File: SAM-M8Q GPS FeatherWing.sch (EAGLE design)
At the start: 24 parts, among them Q1 DMG3415U-7, Q2 2N2222, SW1 KMR2, U1 SAM-M8Q

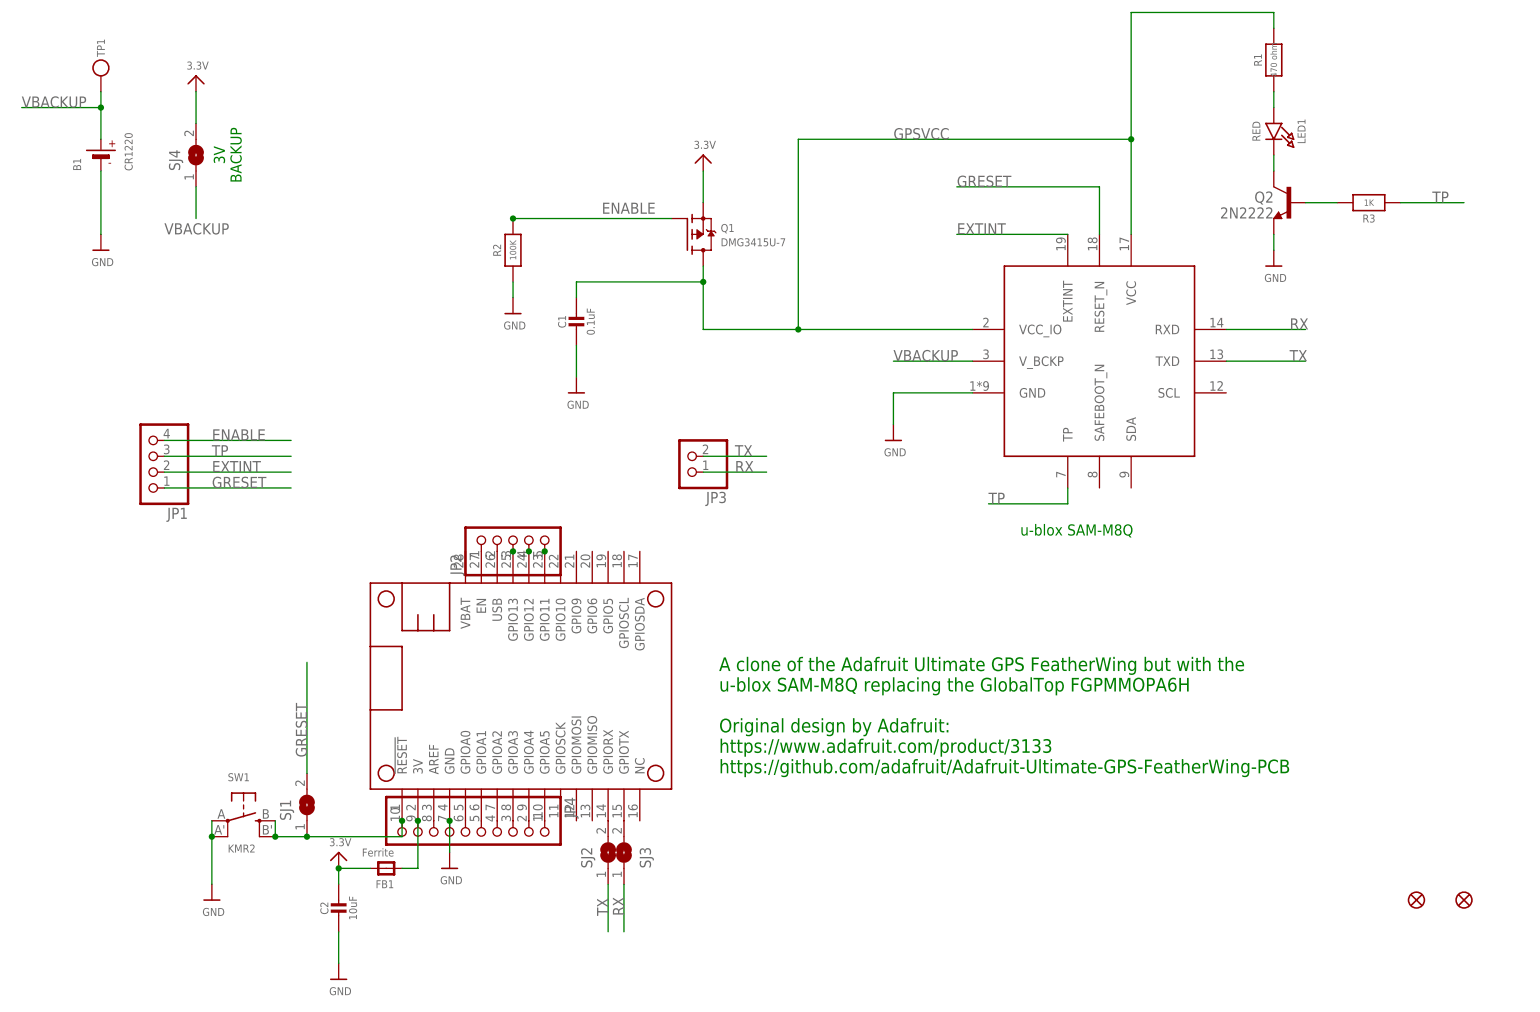
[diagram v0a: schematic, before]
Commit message: Minor tweaks. Included BOM.
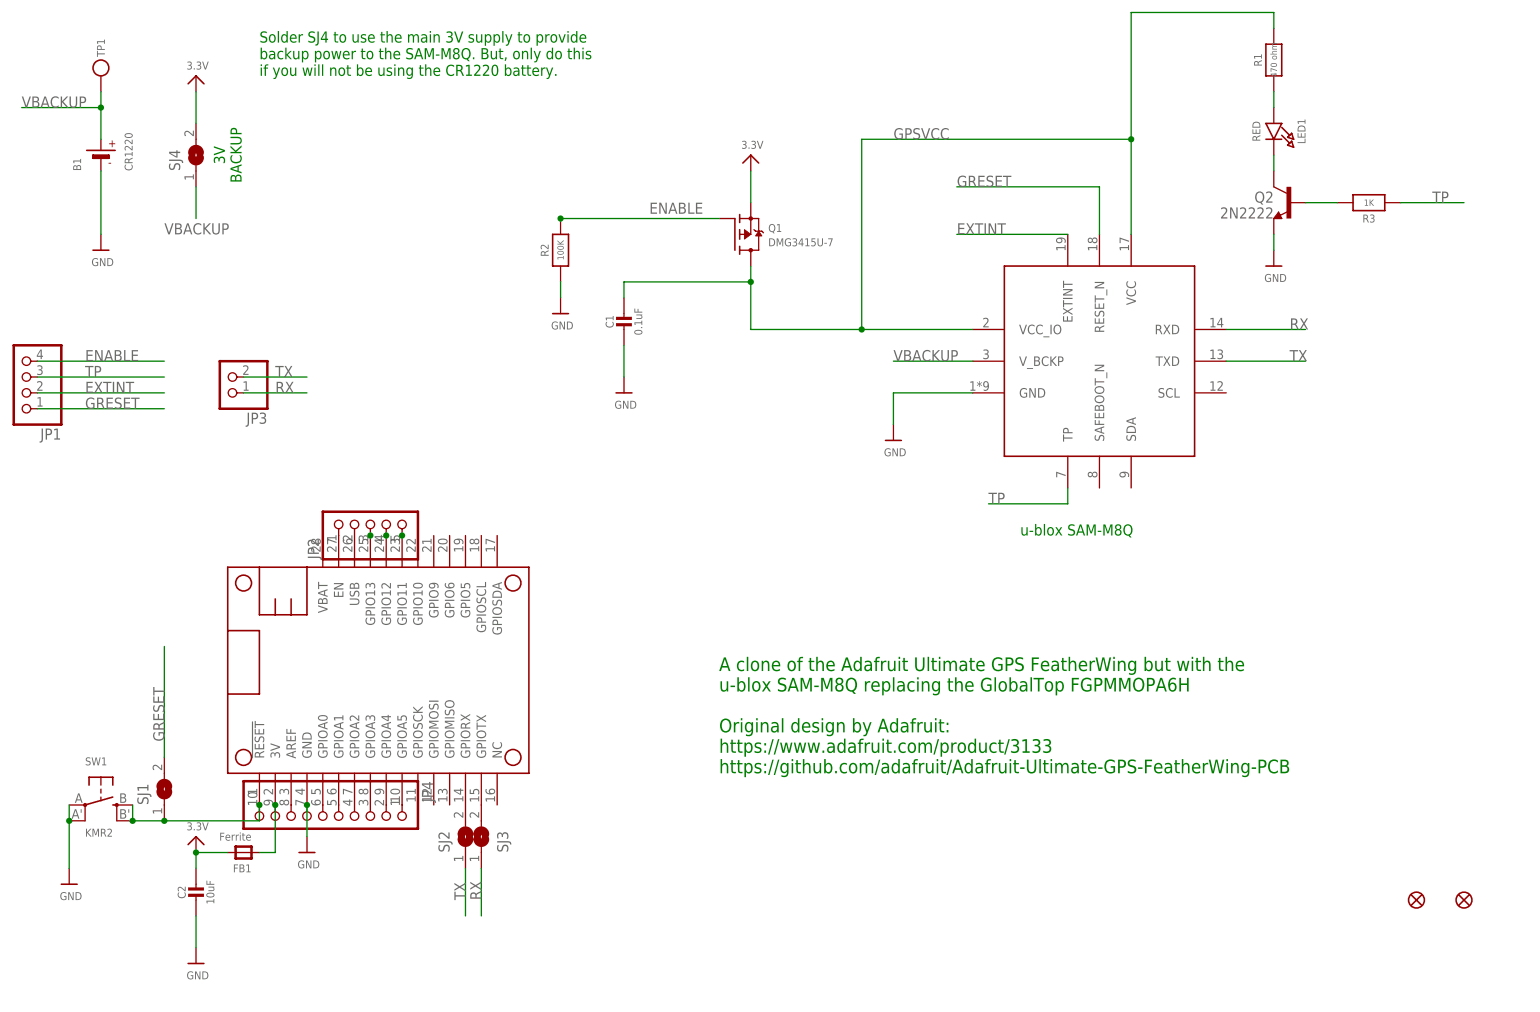
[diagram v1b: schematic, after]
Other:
- note added: "Solder SJ4 to use the main 3V supply to provide backup power to the SAM-M8Q. But, only do this if you will not be using the CR1220 battery."
- moved on the sheet: C1, C2, FB1, JP1, JP2, JP3, JP4, Q1, R2, SJ1, SJ2, SJ3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
